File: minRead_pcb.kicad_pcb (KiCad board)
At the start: 2 copper layers, 60 x 111.3 mm, 169 parts, among them J1 USB_C_Receptacle, J2 FH34SRJ-24S-0.5SH_50_, J3 FH34SRJ-6S-0.5SH_50_, J4 FH34SRJ-6S-0.5SH_50_, J5 Conn_01x02, J6 PPPC062LJBN-RC, J7 Micro_SD_Card, Q1 FS8205A, Q12 MMBT3904, Q13 MMBT3904, Q14 AO3419, Q15 MMBT3906, Q3 AO3419, Q4 BSS138, Q5 BSS138, Q6 BSS138, Q7 AO3419, Q8 AO3419, Q9 BSS138, SW1 SW_Push, SW10 SW_Push, SW11 SW_Push, SW2 SW_Push, SW3 SW_Push, SW4 SW_Push, SW5 SW_Push, SW6 SW_Push, SW7 SW_Push, SW8 SW_Push, SW9 SW_Push, U1 TPD4E1U06DBVR, U10 AP3031KTR, U11 TP4056-42-ESOP8, U12 74LVC1G04, U13 DS3231MZ, U2 TPS2116DRL, U3 AP2112K-3.3, U4 ESP32-S3-WROOM-1, U5 DW01A, U6 TPD4E1U06DBVR, U7 TPD4E1U06DBVR, U8 TPD4E1U06DBVR, U9 TPD4E1U06DBVR

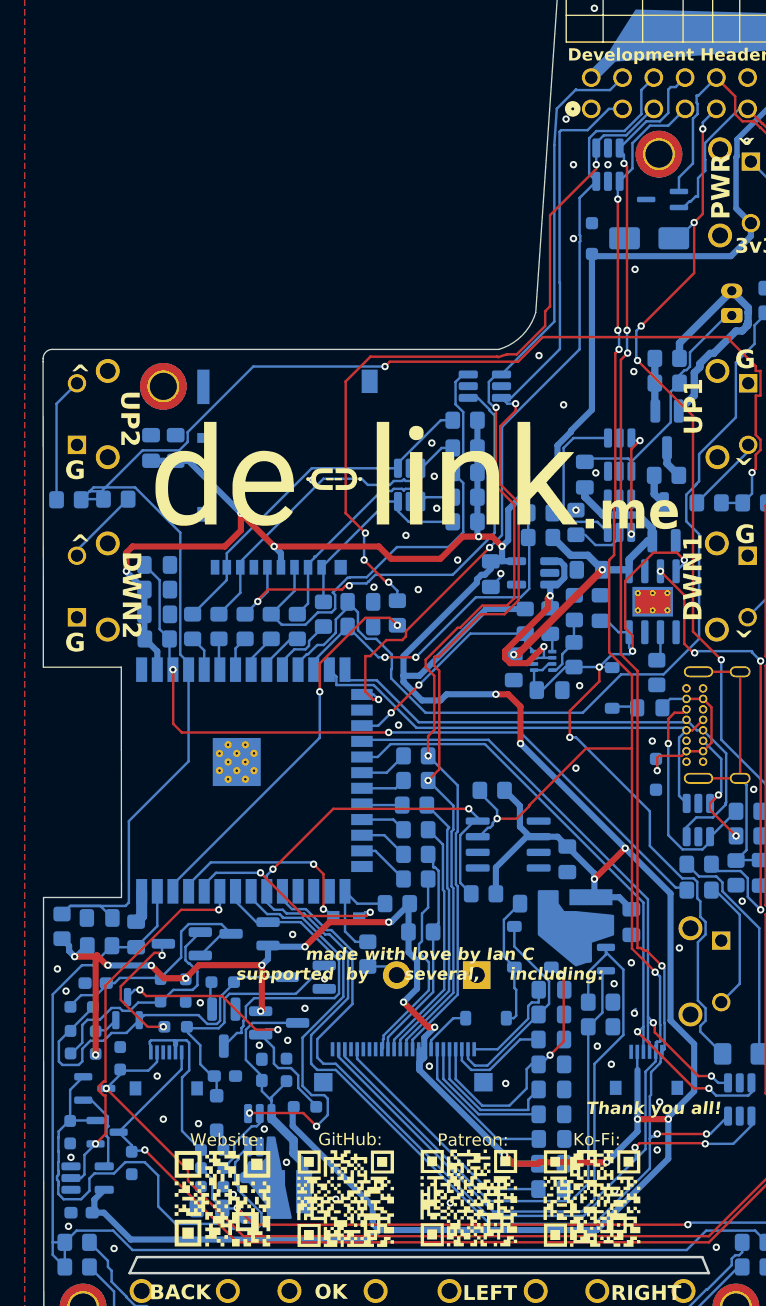
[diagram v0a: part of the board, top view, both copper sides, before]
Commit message: - added LED_ACTIVATE net to proper spot for transistor latch mechanism - added moved 1M ground bleed to SENSE_N instead of 3V3 - removed SPI signals from external header - added GPIO3, GPIO46, GPIO2 to external header with 33ohm series resistors - added P+ to external header with TS05D ESD protection diode - replaced inductor with molded inductor for LED driver (noise reduction) - replaced output cap for LED driver with tantalum cap (noise reduction) - cleaned up unconnected nets - todo: silkscreen (again), EMI stuff, etc
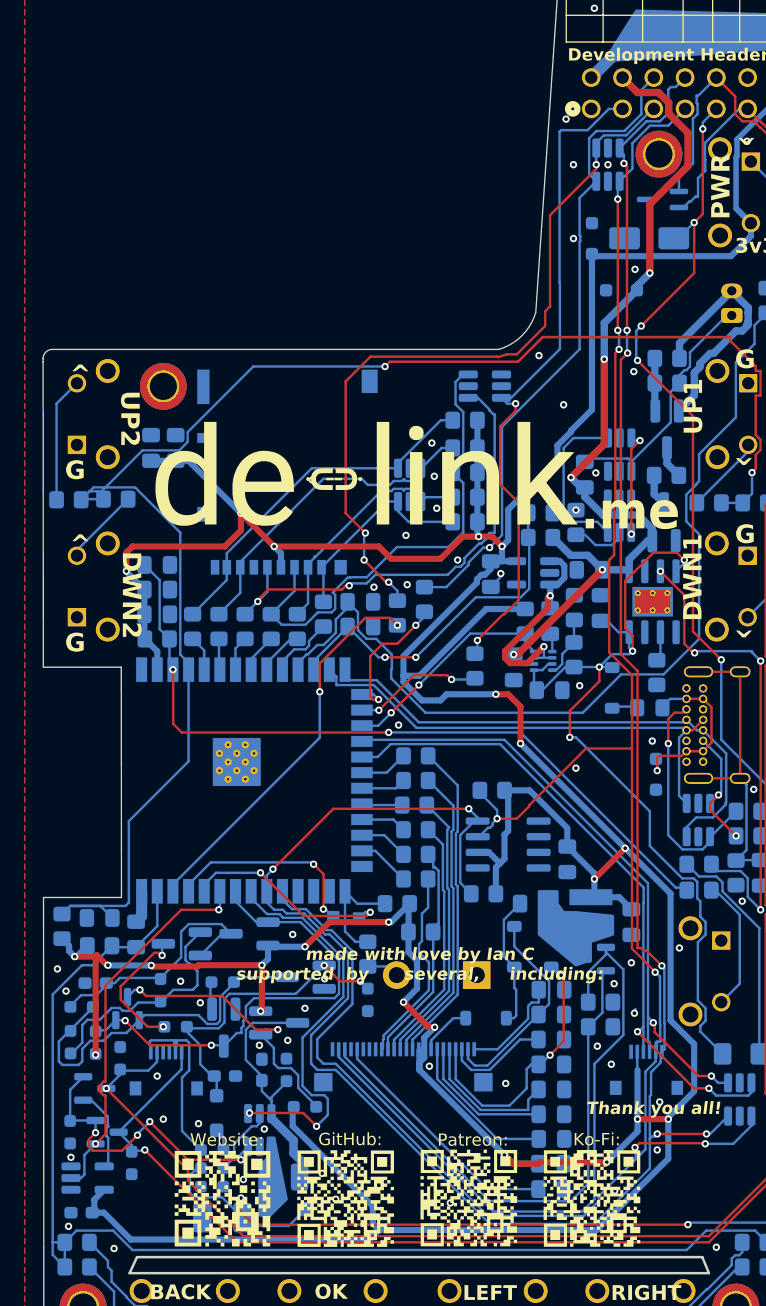
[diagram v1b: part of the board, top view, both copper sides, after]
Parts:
- added CR3: TSD05CDYFR, Diode_SMD:D_SOD-323_HandSoldering, B.Cu at (91.2, 62.7)
- added R68: 33, Resistor_SMD:R_0805_2012Metric_Pad1.20x1.40mm_HandSolder, B.Cu at (75.2, 87.8)
- added R69: 33, Resistor_SMD:R_0805_2012Metric_Pad1.20x1.40mm_HandSolder, B.Cu at (79.3, 93.2)
- C30: value 22u -> 0.1u
- C9: value 4.7u -> 1u; footprint Capacitor_SMD:C_0805_2012Metric_Pad1.18x1.45mm_HandSolder -> Capacitor_Tantalum_SMD:CP_EIA-3528-21_Kemet-B_HandSolder
- L2: value 22u -> 4.7u; footprint srn3010C-100m:IND_SRN3010C-100M -> Inductor_SMD:L_1008_2520Metric_Pad1.43x2.20mm_HandSolder
- R40: value 10k -> 100k
- moved R17 14.8 mm to (70.6, 120.3)
- moved D7 3.20 mm to (63.9, 137.3), turned to 180 degrees
- moved C9 1.29 mm to (58.8, 138.0), turned to 180 degrees
- moved L2 1.26 mm to (63.9, 134.7)
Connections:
- C9 pad 1: GND -> LED_SW
- C9 pad 2: LED_SW -> GND
- J6 pad 2: SPI_SCK -> UNUSED_GPIO_46
- J6 pad 3: SPI_MISO -> UNUSED_GPIO_2
- J6 pad 8: SPI_MOSI -> P+
- Q9 pad 2: Net-(Q9-S) -> LED_ACTIVATE
- R17 pad 1: 3V3 -> /SENSE_N
- R39 pad 1: Net-(Q9-S) -> LED_ACTIVATE
- R65 pad 1: SPI_MISO -> UNUSED_GPIO_2
- U13 pad 2: 3V3 -> GND
- U13 pad 6: GND -> 3V3
- U4 pad 15: UNUSED_GPIO_3 -> Net-(U4-IO3)
- U4 pad 16: unconnected-(U4-IO46-Pad16) -> Net-(U4-IO46)
- U4 pad 26: unconnected-(U4-IO45-Pad26) -> SPI_MISO
- U8 pad 1: SPI_MISO -> UNUSED_GPIO_2
- U9 pad 4: SPI_MOSI -> unconnected-(U9-Pad4)
- U9 pad 6: SPI_SCK -> UNUSED_GPIO_46
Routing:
- net SPI_SCK: track 92.0 -> 24.4 mm, vias 2 -> 0
- net SPI_MOSI: track 93.6 -> 26.5 mm, vias 2 -> 0
- net UNUSED_GPIO_2: track 0.00 -> 60.2 mm, vias 0 -> 4
- net SPI_MISO: track 60.2 -> 0.00 mm, vias 4 -> 0
- net UNUSED_GPIO_46: track 0.00 -> 54.2 mm, vias 0 -> 2
- net P+: track 32.4 -> 73.5 mm, vias 2 -> 5
- net Net-(Q5-S): track 42.6 -> 24.5 mm, vias 0 -> 4
- net UNUSED_GPIO_3: track 65.4 -> 52.3 mm, vias 2 -> 1
- net Net-(U4-IO3): track 0.00 -> 11.8 mm, vias 0 -> 2
- net LED_ACTIVATE: track 26.1 -> 37.7 mm, vias 0 -> 2
- net Net-(U4-IO46): track 0.00 -> 10.5 mm, vias 0 -> 2
- net LED_SW: track 166.8 -> 174.5 mm
- net /SENSE_N: track 21.2 -> 25.5 mm, vias 0 -> 2
- net 3V3: track 416.0 -> 419.6 mm, vias 24 -> 23
- net Net-(Q9-S): track 1.98 -> 0.00 mm
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
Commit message: Swap AP3031 -> TPS923610DRLR, add SW net-class
- add SW net-class and assignments (3031_SW, LED_SW, EINK_SW) in .kicad_pro
- remove AP3031 symbol library (AP3031.kicad_sym/.bak) + sym-lib-table entry
- add TPS923610DRLR: symbol, footprint (U_DRL0006A_6L_TEX + L/M variants),
  and SOT563 3D model; registered in sym-lib-table and fp-lib-table
- schematic/board design updates
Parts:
- removed D7: B5819W, Diode_SMD:D_SOD-123
- removed D9: BZT52C22, Diode_SMD:D_SOD-123F
- removed Q12, Q13: MMBT3904, Package_TO_SOT_SMD:SOT-23_Handsoldering
- removed Q14: AO3419, Package_TO_SOT_SMD:SOT-23_Handsoldering
- removed Q15: MMBT3906, Package_TO_SOT_SMD:SOT-23_Handsoldering
- removed Q9: BSS138, Package_TO_SOT_SMD:SOT-23
- added C31: 10n, Capacitor_SMD:C_0805_2012Metric_Pad1.18x1.45mm_HandSolder, B.Cu at (57.1, 120.3)
- added R70: 100k, Resistor_SMD:R_0805_2012Metric_Pad1.20x1.40mm_HandSolder, B.Cu at (151.3, 106.4)
- added R71: 22k, Resistor_SMD:R_0805_2012Metric_Pad1.20x1.40mm_HandSolder, B.Cu at (151.3, 109.3)
- added R72: 10k, Resistor_SMD:R_0805_2012Metric_Pad1.20x1.40mm_HandSolder, B.Cu at (151.3, 112.3)
- added R73: 0, Resistor_SMD:R_0805_2012Metric_Pad1.20x1.40mm_HandSolder, B.Cu at (151.3, 115.2)
- added R74: 0, Resistor_SMD:R_0805_2012Metric_Pad1.20x1.40mm_HandSolder, B.Cu at (151.3, 118.2)
- added TP3: TestPoint, Connector_PinHeader_2.54mm:PinHeader_1x01_P2.54mm_Vertical, B.Cu at (146.6, 107.2)
- added TP4: TestPoint, Connector_PinHeader_2.54mm:PinHeader_1x01_P2.54mm_Vertical, B.Cu at (146.6, 111.8)
- added TP5: TestPoint, Connector_PinHeader_2.54mm:PinHeader_1x01_P2.54mm_Vertical, B.Cu at (146.6, 116.4)
- C12, C24: footprint Capacitor_SMD:C_0603_1608Metric_Pad1.08x0.95mm_HandSolder -> Capacitor_SMD:C_0805_2012Metric_Pad1.18x1.45mm_HandSolder
- C21: value 1n -> 1u; footprint Capacitor_SMD:C_0603_1608Metric_Pad1.08x0.95mm_HandSolder -> Capacitor_SMD:C_0805_2012Metric_Pad1.18x1.45mm_HandSolder
- C23: value 100n -> 2.2n; footprint Capacitor_SMD:C_0603_1608Metric_Pad1.08x0.95mm_HandSolder -> Capacitor_SMD:C_0805_2012Metric_Pad1.18x1.45mm_HandSolder
- C9: footprint Capacitor_Tantalum_SMD:CP_EIA-3528-21_Kemet-B_HandSolder -> Capacitor_SMD:C_0805_2012Metric_Pad1.18x1.45mm_HandSolder
- R17: value 1M -> 100k; footprint Resistor_SMD:R_0603_1608Metric_Pad0.98x0.95mm_HandSolder -> Resistor_SMD:R_0805_2012Metric_Pad1.20x1.40mm_HandSolder
- R37, R40, R49, R50: footprint Resistor_SMD:R_0603_1608Metric_Pad0.98x0.95mm_HandSolder -> Resistor_SMD:R_0805_2012Metric_Pad1.20x1.40mm_HandSolder
- R39: value 100k -> 1M; footprint Resistor_SMD:R_0603_1608Metric_Pad0.98x0.95mm_HandSolder -> Resistor_SMD:R_0805_2012Metric_Pad1.20x1.40mm_HandSolder
- R41: value 4.7k -> 120k; footprint Resistor_SMD:R_0603_1608Metric_Pad0.98x0.95mm_HandSolder -> Resistor_SMD:R_0805_2012Metric_Pad1.20x1.40mm_HandSolder
- R42: value 330 -> 0; footprint Resistor_SMD:R_0603_1608Metric_Pad0.98x0.95mm_HandSolder -> Resistor_SMD:R_0805_2012Metric_Pad1.20x1.40mm_HandSolder
- R43, R52: value 22k -> 0; footprint Resistor_SMD:R_0603_1608Metric_Pad0.98x0.95mm_HandSolder -> Resistor_SMD:R_0805_2012Metric_Pad1.20x1.40mm_HandSolder
- R44, R45: value 10k -> 0; footprint Resistor_SMD:R_0603_1608Metric_Pad0.98x0.95mm_HandSolder -> Resistor_SMD:R_0805_2012Metric_Pad1.20x1.40mm_HandSolder
- R46: value 47k' -> 0; footprint Resistor_SMD:R_0603_1608Metric_Pad0.98x0.95mm_HandSolder -> Resistor_SMD:R_0805_2012Metric_Pad1.20x1.40mm_HandSolder
- R58: value 100k -> 0
- R59: value 1k -> 2k
- R66: value 680k -> 0; footprint Resistor_SMD:R_0603_1608Metric_Pad0.98x0.95mm_HandSolder -> Resistor_SMD:R_0805_2012Metric_Pad1.20x1.40mm_HandSolder
- R67: value 1M -> 56k; footprint Resistor_SMD:R_0603_1608Metric_Pad0.98x0.95mm_HandSolder -> Resistor_SMD:R_0805_2012Metric_Pad1.20x1.40mm_HandSolder
- U10: value AP3031KTR -> TPS923610DRLR; footprint Package_TO_SOT_SMD:SOT-23-6_Handsoldering -> TPS923610DRLR:U_DRL0006A_6L_TEX-M
- moved R42 113.5 mm to (160.8, 115.2), turned to 180 degrees
- moved R39 113.2 mm to (160.8, 109.3), turned to 180 degrees
- moved R45 110.9 mm to (156.0, 106.4), turned to 180 degrees
- moved R44 105.8 mm to (160.8, 121.1)
- moved R41 104.8 mm to (160.8, 112.3)
- moved R46 102.7 mm to (156.0, 109.3), turned to 180 degrees
- moved R43 101.9 mm to (160.8, 118.2), turned to 180 degrees
- moved R66 99.3 mm to (156.0, 118.2), turned to 180 degrees
- moved R67 99.1 mm to (156.0, 121.1)
- moved U10 99.0 mm to (160.7, 124.5), turned to 180 degrees
- moved C23 98.3 mm to (146.5, 126.2)
- moved R52 93.0 mm to (156.0, 112.3), turned to 180 degrees
- moved R17 91.2 mm to (160.8, 106.4), turned to 180 degrees
- moved C9 89.5 mm to (146.5, 120.2)
- moved C21 87.6 mm to (146.5, 123.2)
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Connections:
- C21 pad 1: GND -> 3V3
- C21 pad 2: /SENSE_N -> GND
- C23 pad 1: /LATCH_PWR -> USB_STAT
- C9 pad 1: LED_SW -> GND
- C9 pad 2: GND -> LED_SW
- J4 pad 2: 3V3 -> /PIN_2
- J4 pad 4: TP_INT -> /PIN_4
- J4 pad 5: I2C_SDA -> /PIN_5
- J4 pad 6: I2C_SCL -> /PIN_6
- J6 pad 3: UNUSED_GPIO_2 -> UNUSED_GPIO_45
- Q7 pad 1: Net-(Q7-G) -> LED_ACTIVATE
- R17 pad 1: /SENSE_N -> ST
- R17 pad 2: GND -> USB_STAT
- R39 pad 1: LED_ACTIVATE -> LED_SW
- R39 pad 2: 3V3 -> LED_MONIT
- R40 pad 1: Net-(Q7-G) -> LED_ACTIVATE
- R41 pad 1: Net-(D9-K) -> LED_MONIT
- R41 pad 2: LED_SW -> GND
- R42 pad 1: /LATCH_PWR -> 3V3
- R42 pad 2: /ISO_GATE -> /PIN_2
- R43 pad 1: Net-(Q13-B) -> TP_INT
- R43 pad 2: /ISO_GATE -> /PIN_2
- R44 pad 1: /SENSE_N -> TP_INT
- R44 pad 2: Net-(Q15-C) -> /PIN_4
- R45 pad 1: /ISO_GATE -> I2C_SCL
- R45 pad 2: Net-(Q15-B) -> /PIN_6
- R46 pad 1: Net-(Q15-B) -> I2C_SDA
- R46 pad 2: /LATCH_PWR -> /PIN_5
- R52 pad 1: GND -> I2C_SCL
- R52 pad 2: Net-(Q7-D) -> /PIN_6
- R58 pad 1: USB_STAT -> I2C_SDA
- R58 pad 2: 3V3 -> /PIN_5
- R59 pad 2: Net-(U11-~{CHRG}) -> GND
- R65 pad 1: UNUSED_GPIO_2 -> Net-(U4-IO46)
- R65 pad 2: Net-(U4-IO2) -> UNUSED_GPIO_46
- R66 pad 1: LED_SW -> 3V3
- R66 pad 2: /OVP -> /PIN_4
- R67 pad 1: /OVP -> CHRG
- R67 pad 2: GND -> USB_STAT
- R69 pad 1: Net-(U4-IO46) -> Net-(U4-IO45)
- R69 pad 2: UNUSED_GPIO_46 -> UNUSED_GPIO_45
- SW7 pad 1: GND -> Net-(R73-Pad2)
- U10 pad 1: 3031_SW -> Net-(Q7-D)
- U10 pad 2: GND -> PWM_LED
- U10 pad 4: PWM_LED -> GND
- U10 pad 5: /OVP -> LED_SW
- U10 pad 6: Net-(Q7-D) -> 3031_SW
- U11 pad 6: unconnected-(U11-~{STDBY}-Pad6) -> STDBY
- U11 pad 7: Net-(U11-~{CHRG}) -> CHRG
- U2 pad 8: USB_STAT -> ST
- U4 pad 17: USB_STAT -> LED_MONIT
- U4 pad 26: SPI_MISO -> Net-(U4-IO45)
- U4 pad 28: unconnected-(U4-IO35-Pad28) -> IO35_PSRAM
- U4 pad 29: unconnected-(U4-IO36-Pad29) -> IO36_PSRAM
- U4 pad 30: unconnected-(U4-IO37-Pad30) -> IO37_PSRAM
- U4 pad 38: Net-(U4-IO2) -> USB_STAT
- U7 pad 1: TP_INT -> /PIN_4
- U7 pad 4: I2C_SDA -> /PIN_5
- U7 pad 6: I2C_SCL -> /PIN_6
- U8 pad 1: UNUSED_GPIO_2 -> UNUSED_GPIO_45
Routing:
- net UNUSED_GPIO_2: track 60.2 -> 0.00 mm, vias 4 -> 0
- net Net-(U4-IO46): track 10.5 -> 70.7 mm, vias 2 -> 6
- net Net-(U11-~{CHRG}): track 40.3 -> 0.00 mm, vias 4 -> 0
- net GND: track 10.3 -> 50.5 mm, vias 58 -> 56
- net UNUSED_GPIO_46: track 54.2 -> 85.7 mm, vias 2 -> 4
- net Net-(U4-IO2): track 31.5 -> 0.00 mm, vias 2 -> 0
- net /ISO_GATE: track 29.5 -> 0.00 mm
- net LED_ACTIVATE: track 37.7 -> 9.88 mm, vias 2 -> 0
- net /SENSE_N: track 25.5 -> 0.00 mm, vias 2 -> 0
- net Net-(Q7-G): track 23.7 -> 0.00 mm, vias 2 -> 0
- net LED_SW: track 174.5 -> 151.3 mm
- net PWM_LED: track 32.9 -> 11.8 mm
- net /LATCH_PWR: track 20.7 -> 0.00 mm
- net 3V3: track 419.6 -> 399.9 mm, vias 23 -> 21
- net Net-(Q15-B): track 18.9 -> 0.00 mm
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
